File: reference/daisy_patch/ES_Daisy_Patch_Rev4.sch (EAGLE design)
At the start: 214 parts, among them Q1 MMBT3904, Q2 MMBT3904, U1 AP1509-33SG-13, U11 TL074, U13 TL074, U14 TL074, U15 OPTOISOLATOR_H11L1M, U16 TL074, U2 AK4556, U3 MICRO_SD_CARDCENTERED, U4 TL074, U5 TL074, U6 LM4040-10V, U7 MCP6004

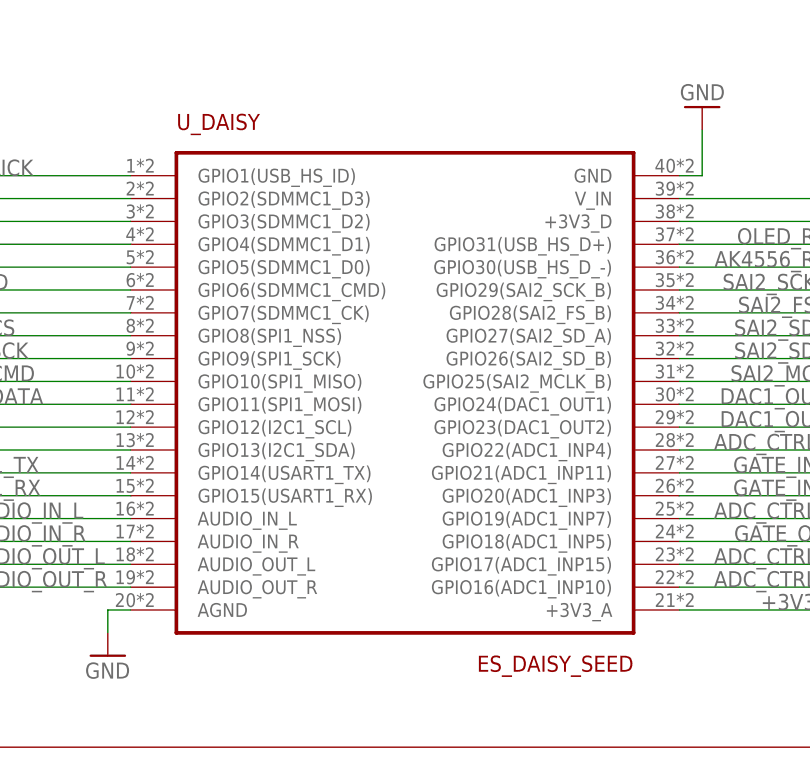
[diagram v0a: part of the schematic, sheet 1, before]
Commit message: updated Daisy symbol in DaisyPatch sch.
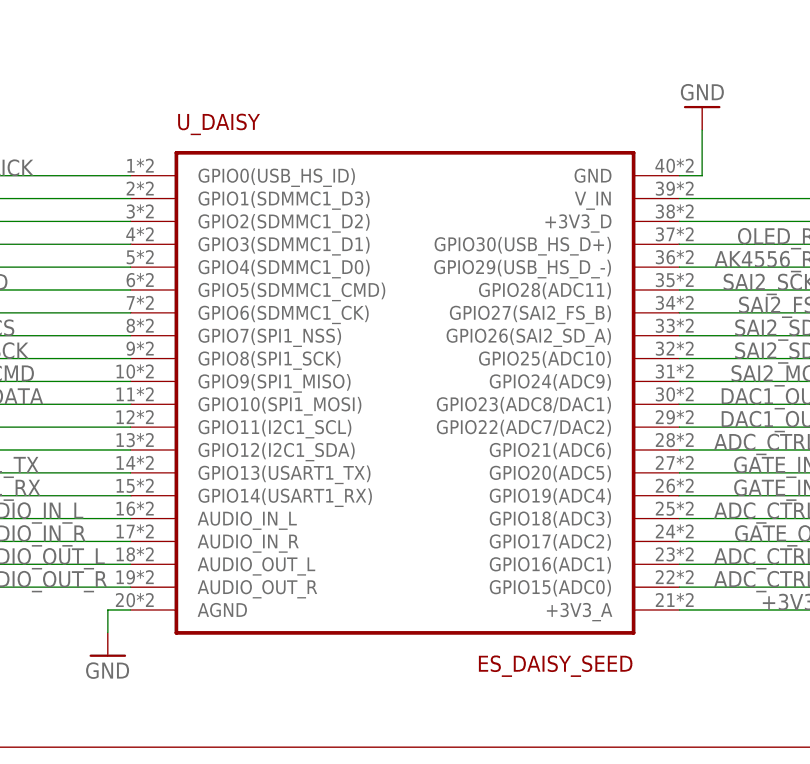
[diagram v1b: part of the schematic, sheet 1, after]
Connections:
- net ADC_CTRL_1: now also U_DAISY.GPIO15(ADC0); no longer U_DAISY.GPIO16(ADC1_INP10)
- net ADC_CTRL_2: now also U_DAISY.GPIO16(ADC1); no longer U_DAISY.GPIO17(ADC1_INP15)
- net ADC_CTRL_3: now also U_DAISY.GPIO21(ADC6); no longer U_DAISY.GPIO22(ADC1_INP4)
- net ADC_CTRL_4: now also U_DAISY.GPIO18(ADC3); no longer U_DAISY.GPIO19(ADC1_INP7)
- net AK4556_RST: now also U_DAISY.GPIO29(USB_HS_D_-); no longer U_DAISY.GPIO30(USB_HS_D_-)
- net DAC1_OUT1: now also U_DAISY.GPIO23(ADC8/DAC1); no longer U_DAISY.GPIO24(DAC1_OUT1)
- net DAC1_OUT2: now also U_DAISY.GPIO22(ADC7/DAC2); no longer U_DAISY.GPIO23(DAC1_OUT2)
- net ENC_A: now also U_DAISY.GPIO12(I2C1_SDA); no longer U_DAISY.GPIO13(I2C1_SDA)
- net ENC_B: now also U_DAISY.GPIO11(I2C1_SCL); no longer U_DAISY.GPIO12(I2C1_SCL)
- net ENC_CLICK: now also U_DAISY.GPIO0(USB_HS_ID); no longer U_DAISY.GPIO1(USB_HS_ID)
- net GATE_IN_1: now also U_DAISY.GPIO20(ADC5); no longer U_DAISY.GPIO21(ADC1_INP11)
- net GATE_IN_2: now also U_DAISY.GPIO19(ADC4); no longer U_DAISY.GPIO20(ADC1_INP3)
- net GATE_OUT: now also U_DAISY.GPIO17(ADC2); no longer U_DAISY.GPIO18(ADC1_INP5)
- net OLED_CMD: now also U_DAISY.GPIO9(SPI1_MISO); no longer U_DAISY.GPIO10(SPI1_MISO)
- net OLED_CS: now also U_DAISY.GPIO7(SPI1_NSS); no longer U_DAISY.GPIO8(SPI1_NSS)
- net OLED_DATA: now also U_DAISY.GPIO10(SPI1_MOSI); no longer U_DAISY.GPIO11(SPI1_MOSI)
- net OLED_RST: now also U_DAISY.GPIO30(USB_HS_D+); no longer U_DAISY.GPIO31(USB_HS_D+)
- net OLED_SCK: now also U_DAISY.GPIO8(SPI1_SCK); no longer U_DAISY.GPIO9(SPI1_SCK)
- net SAI2_FS_A: now also U_DAISY.GPIO27(SAI2_FS_B); no longer U_DAISY.GPIO28(SAI2_FS_B)
- net SAI2_MCLK: now also U_DAISY.GPIO24(ADC9); no longer U_DAISY.GPIO25(SAI2_MCLK_B)
- net SAI2_SCK_A: now also U_DAISY.GPIO28(ADC11); no longer U_DAISY.GPIO29(SAI2_SCK_B)
- net SAI2_SD_A: now also U_DAISY.GPIO26(SAI2_SD_A); no longer U_DAISY.GPIO27(SAI2_SD_A)
- net SAI2_SD_B: now also U_DAISY.GPIO25(ADC10); no longer U_DAISY.GPIO26(SAI2_SD_B)
- net SD_CK: now also U_DAISY.GPIO6(SDMMC1_CK); no longer U_DAISY.GPIO7(SDMMC1_CK)
- net SD_CMD: now also U_DAISY.GPIO5(SDMMC1_CMD); no longer U_DAISY.GPIO6(SDMMC1_CMD)
- net SD_D0: now also U_DAISY.GPIO4(SDMMC1_D0); no longer U_DAISY.GPIO5(SDMMC1_D0)
- net SD_D1: now also U_DAISY.GPIO3(SDMMC1_D1); no longer U_DAISY.GPIO4(SDMMC1_D1)
- net SD_D2: now also U_DAISY.GPIO2(SDMMC1_D2); no longer U_DAISY.GPIO3(SDMMC1_D2)
- net SD_D3: now also U_DAISY.GPIO1(SDMMC1_D3); no longer U_DAISY.GPIO2(SDMMC1_D3)
- net USART1_RX: now also U_DAISY.GPIO14(USART1_RX); no longer U_DAISY.GPIO15(USART1_RX)
- net USART1_TX: now also U_DAISY.GPIO13(USART1_TX); no longer U_DAISY.GPIO14(USART1_TX)
